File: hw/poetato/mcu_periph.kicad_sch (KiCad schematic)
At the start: 27 parts, among them Q10 NTK3134N, Q9 NTK3134N, U10 SE051, U11 S25FL064LABMFI013

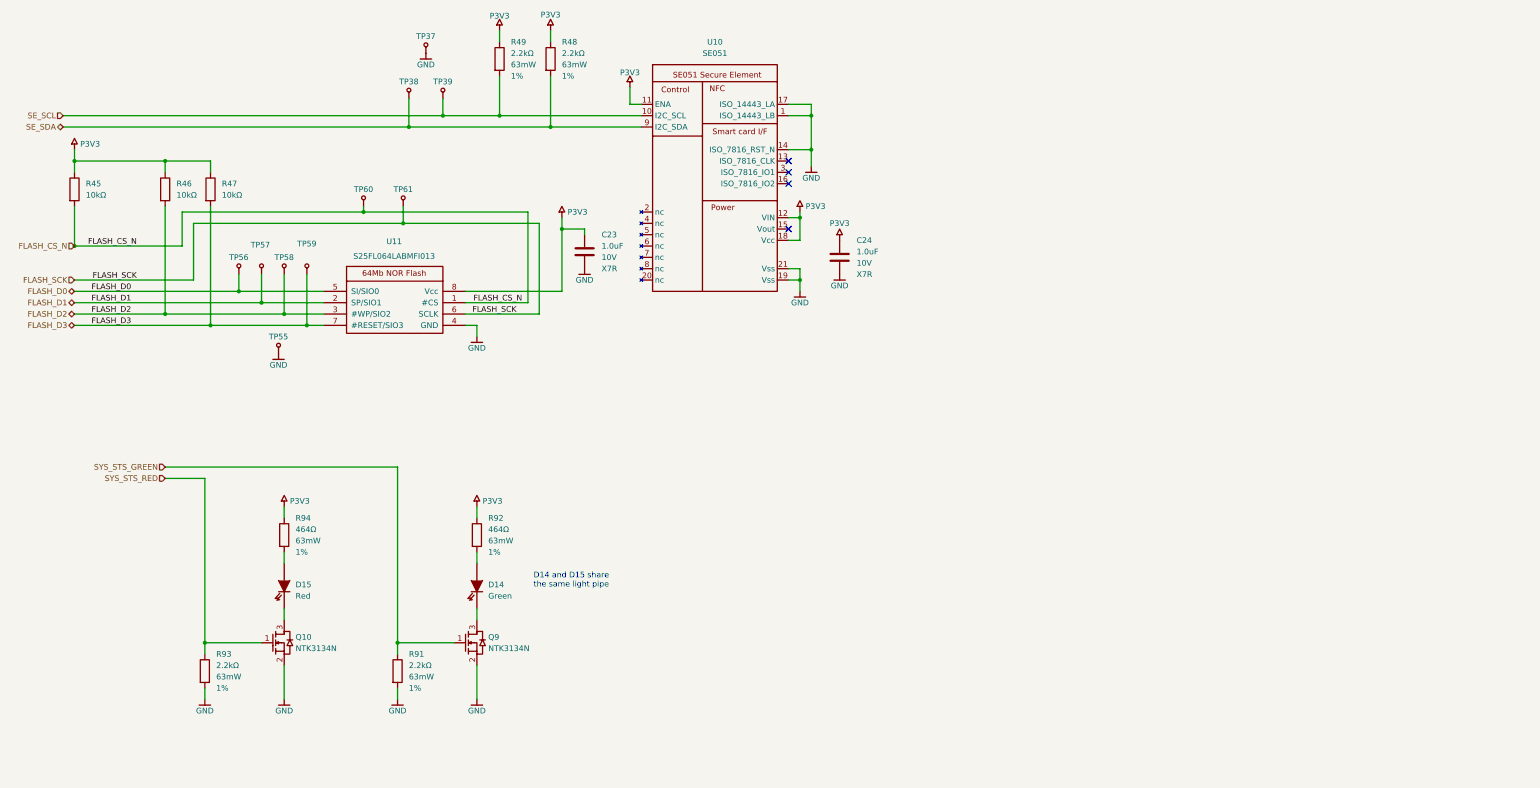
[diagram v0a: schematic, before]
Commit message: hw: schematic touch-ups, J3 updated from library
Layout touch-ups in KiCad. J3 (FTSH-105) pulled from kicadlib 81de170:
pin numbers without leading zeros (01-10 -> 1-10). Otherwise connectivity
and values unchanged; ERC clean. Project file picks up the Peripherals
sheet name.
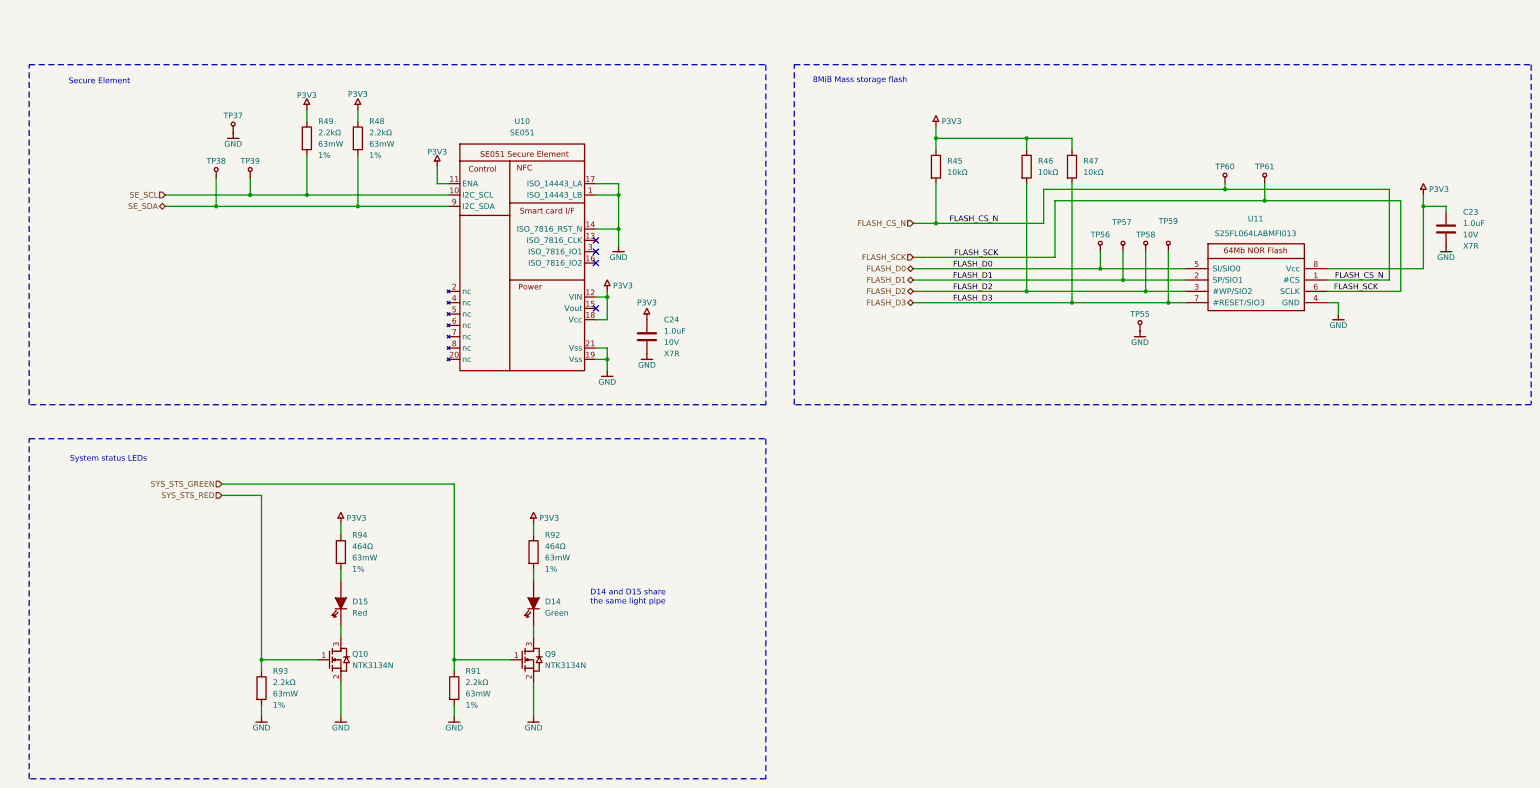
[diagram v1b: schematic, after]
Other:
- note added: "8MiB Mass storage flash"
- note added: "Secure Element"
- note added: "System status LEDs"
- moved on the sheet: C23, C24, D14, D15, Q10, Q9, R45, R46, R47, R48, R49, R91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

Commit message: hw: 2.54 mm block titles, DI sheets on A3
- MCU: RTC block title at 2.54 mm (two lines); its contents move down
  7.62 mm to make room
- Peripherals: the three block titles at 2.54 mm, left-aligned in their frames
- DI: A3 like every other sheet, content placed as on the DO sheets; the
  COOL_POUR ERC exclusion in the project file follows the label

ERC clean, netlist unchanged.
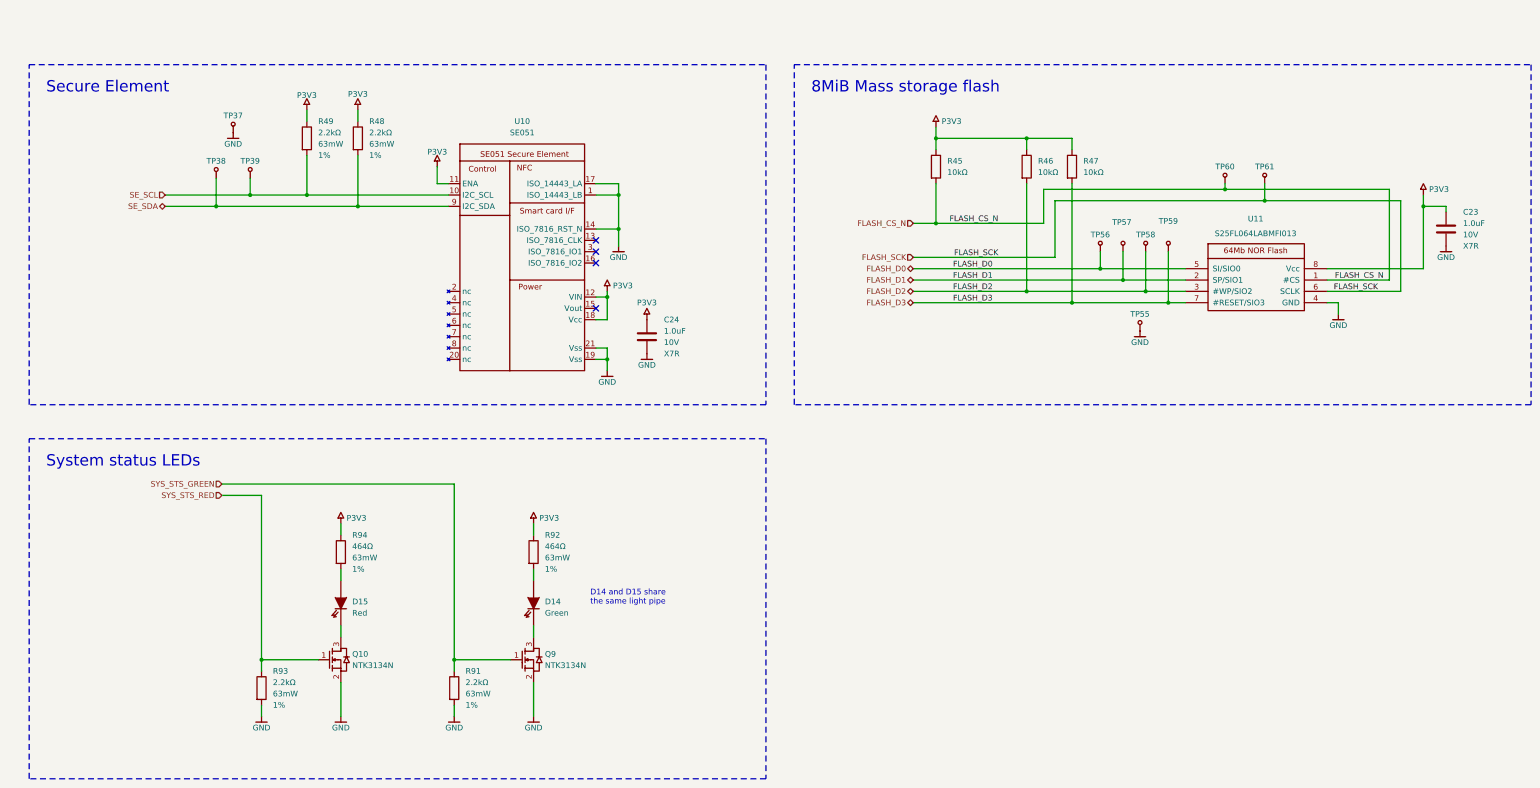
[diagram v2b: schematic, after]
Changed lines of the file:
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@@
 	(text "Secure Element"
 		(exclude_from_sim no)
-		(at 41.148 29.21 0)
+		(at 29.21 30.48 0)
 		(effects
 			(font
-				(size 1.27 1.27)
+				(size 2.54 2.54)
 			)
+			(justify left)
 		)
 	)
 	(text "System status LEDs"
 		(exclude_from_sim no)
-		(at 43.18 113.792 0)
+		(at 29.21 114.3 0)
 		(effects
 			(font
-				(size 1.27 1.27)
+				(size 2.54 2.54)
 			)
+			(justify left)
 		)
 	)
@@
 	(text "8MiB Mass storage flash"
 		(exclude_from_sim no)
-		(at 211.582 28.956 0)
+		(at 200.66 30.48 0)
 		(effects
 			(font
-				(size 1.27 1.27)
+				(size 2.54 2.54)
 			)
+			(justify left)
 		)
 	)
